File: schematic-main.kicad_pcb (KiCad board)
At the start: 2 copper layers, 97.6 x 72.5 mm, 77 parts, among them IC1 LM76202QPWPRQ1, J1 Conn_01x02, J2 Conn_01x03, J3 Conn_01x03_Pin, J6 Conn_01x04, P1 USB_C_Plug_USB2.0, U2 TPS62933, U3 USBLC6-2P6, U4 ESP32-S3FN8, U5 SN65HVD232, U6 PC817, U7 PC817, Y1 Crystal_GND24

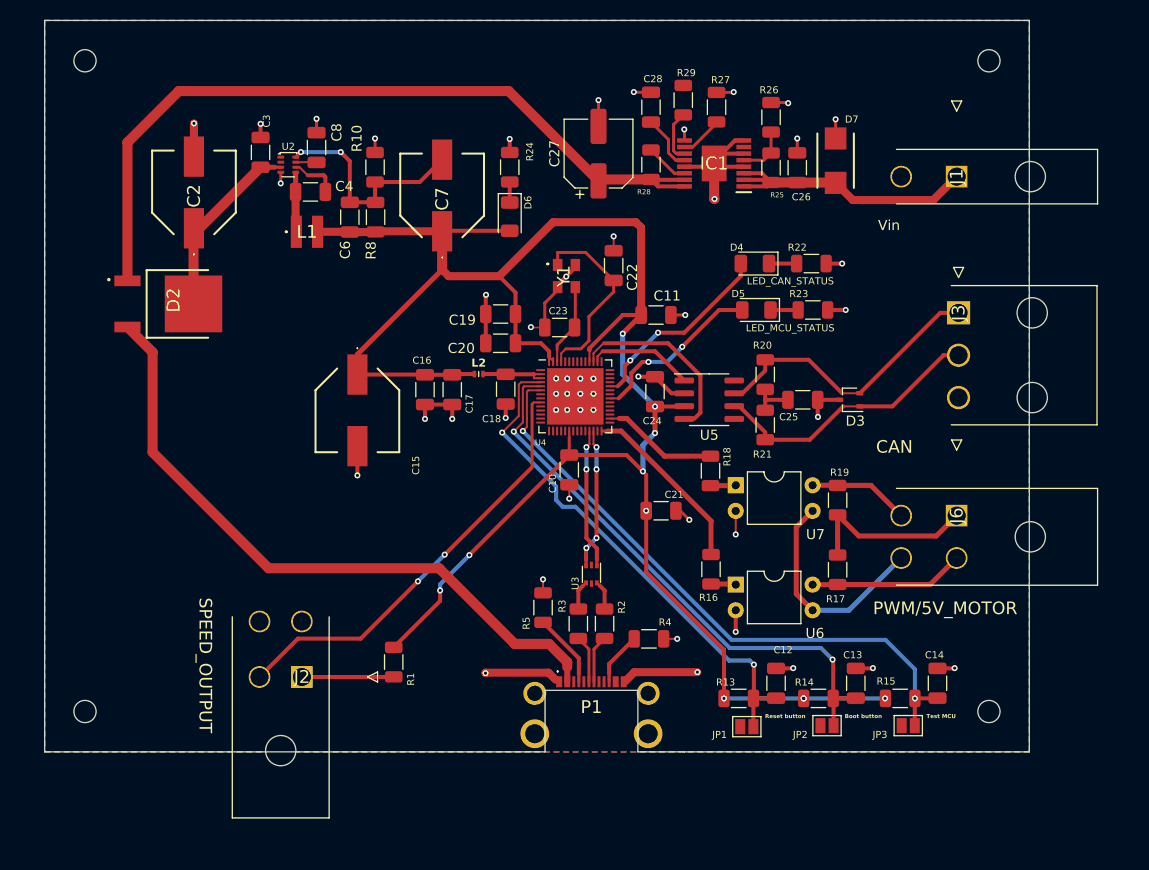
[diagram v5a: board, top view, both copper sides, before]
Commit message: Add test pins for: 3,3V, 5V, 12V and GND
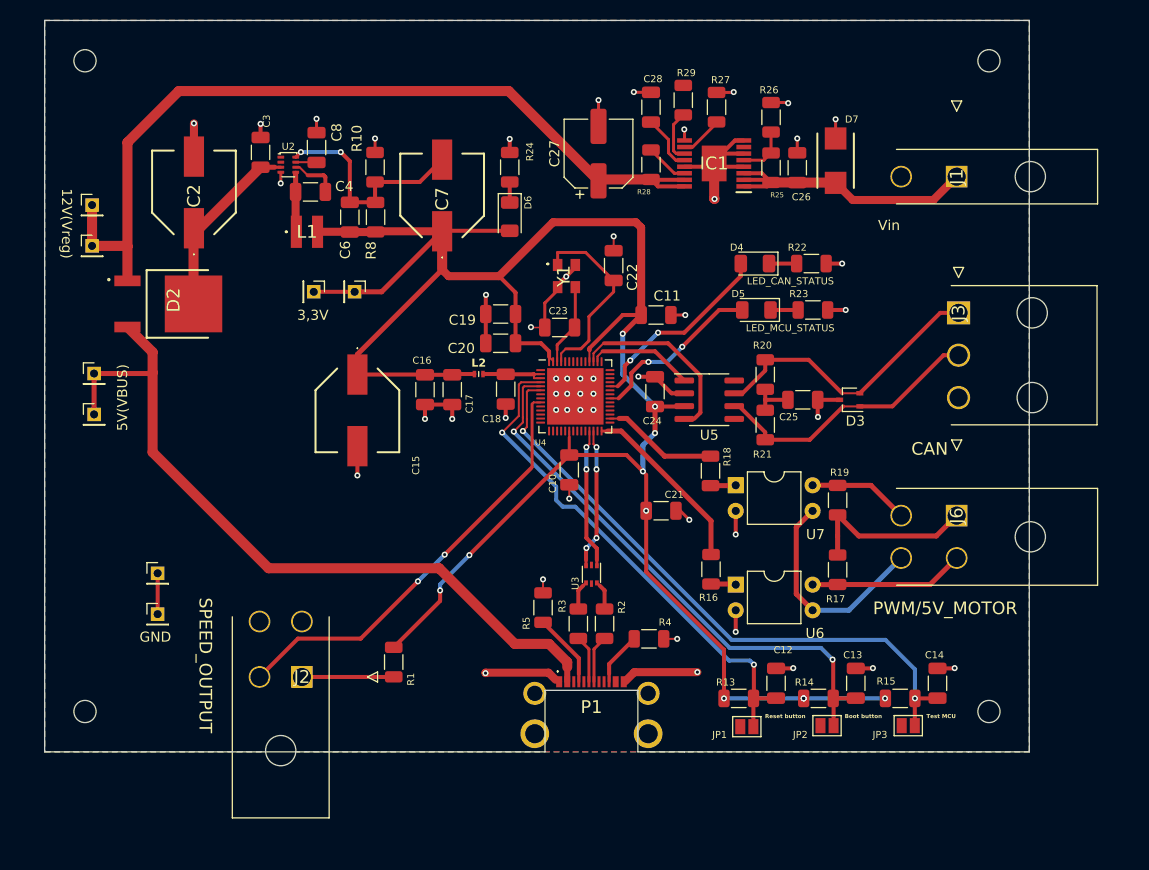
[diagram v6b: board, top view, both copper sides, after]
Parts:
- added TP1: +12V, Connector_PinHeader_2.00mm:PinHeader_1x01_P2.00mm_Vertical, F.Cu at (53.1, 70.0)
- added TP2: +12V, Connector_PinHeader_2.00mm:PinHeader_1x01_P2.00mm_Vertical, F.Cu at (53.1, 74.0)
- added TP3: +5V, Connector_PinHeader_2.00mm:PinHeader_1x01_P2.00mm_Vertical, F.Cu at (53.3, 86.7)
- added TP4: +5V, Connector_PinHeader_2.00mm:PinHeader_1x01_P2.00mm_Vertical, F.Cu at (53.3, 90.8)
- added TP5: +3,3V, Connector_PinHeader_2.00mm:PinHeader_1x01_P2.00mm_Vertical, F.Cu at (79.1, 78.6)
- added TP6: +3,3V, Connector_PinHeader_2.00mm:PinHeader_1x01_P2.00mm_Vertical, F.Cu at (75.1, 78.6)
- added TP7: GND, Connector_PinHeader_2.00mm:PinHeader_1x01_P2.00mm_Vertical, F.Cu at (59.6, 106.5)
- added TP8: GND, Connector_PinHeader_2.00mm:PinHeader_1x01_P2.00mm_Vertical, F.Cu at (59.6, 110.5)
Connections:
- net /Power /Vreg renamed /Vreg
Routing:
- net +3.3V: track 199.7 -> 215.0 mm
- net /VBUS: track 66.7 -> 76.6 mm
- net /Vreg: track 78.4 -> 86.0 mm
- net GND: track 108.9 -> 112.9 mm
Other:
- board text added: "12V(Vreg)"
- board text added: "3,3V"
- board text added: "5V(VBUS)"
- board text added: "GND"

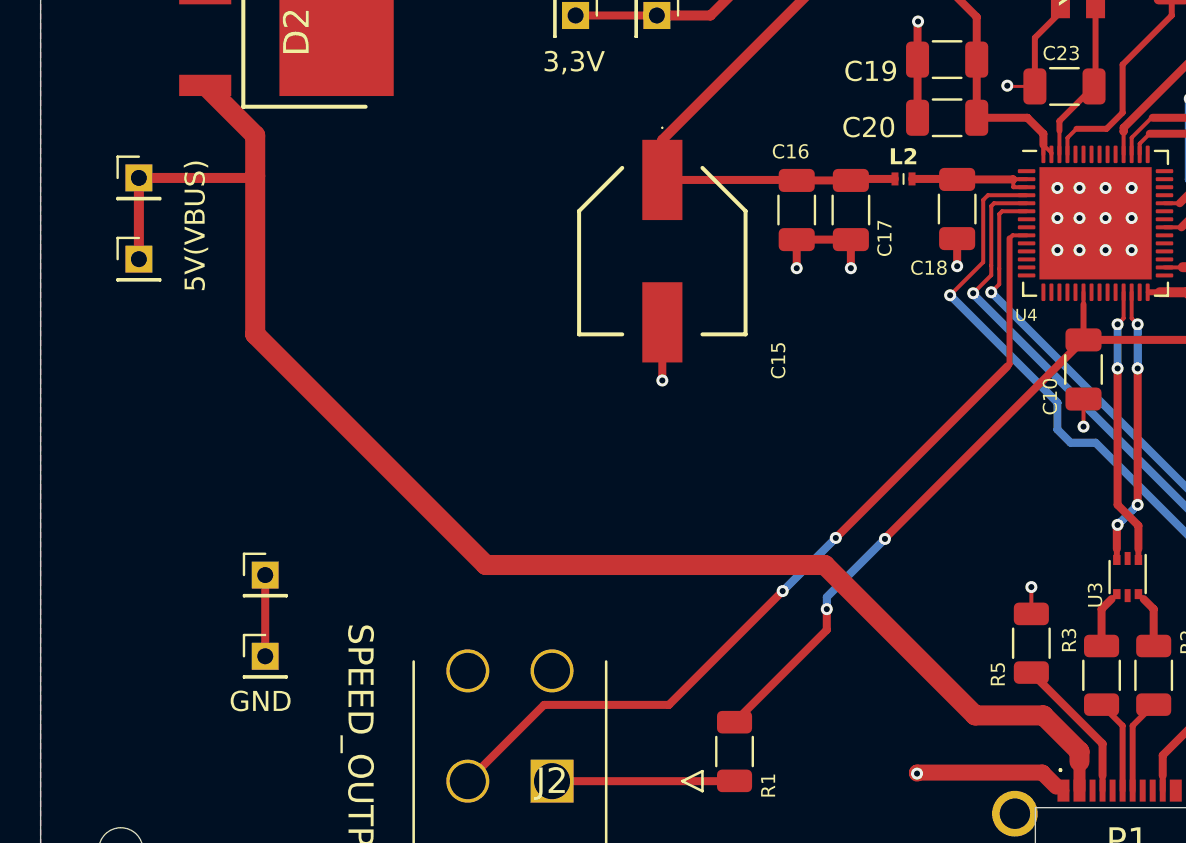
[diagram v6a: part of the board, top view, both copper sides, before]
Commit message: Add test pins for I/O MCU
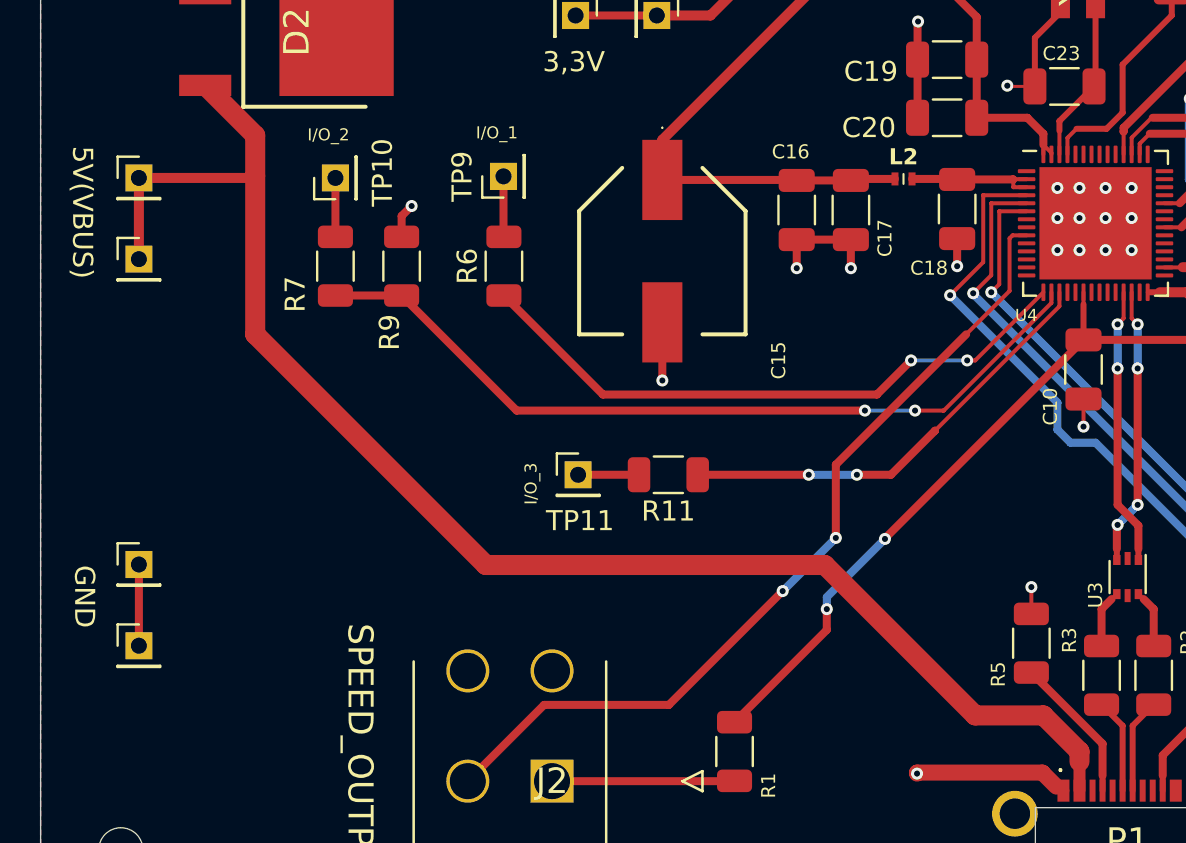
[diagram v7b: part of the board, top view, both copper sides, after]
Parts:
- added R11: R, Resistor_SMD:R_1206_3216Metric, F.Cu at (79.7, 101.5)
- added R6: R, Resistor_SMD:R_1206_3216Metric, F.Cu at (71.5, 91.1)
- added R7: R, Resistor_SMD:R_1206_3216Metric, F.Cu at (63.1, 91.1)
- added R9: R, Resistor_SMD:R_1206_3216Metric, F.Cu at (66.4, 91.1)
- added TP10: I/O_2, Connector_PinHeader_2.00mm:PinHeader_1x01_P2.00mm_Vertical, F.Cu at (63.1, 86.7)
- added TP11: I/O_3, Connector_PinHeader_2.00mm:PinHeader_1x01_P2.00mm_Vertical, F.Cu at (75.2, 101.5)
- added TP9: I/O_1, Connector_PinHeader_2.00mm:PinHeader_1x01_P2.00mm_Vertical, F.Cu at (71.5, 86.6)
- moved TP7 6.32 mm to (53.3, 106.0)
- moved TP8 6.32 mm to (53.3, 110.0)
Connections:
- U4 pad 15: unconnected-(U4-GPIO10/ADC1_CH9-Pad15) -> /IO/I/O_1_MCU
- U4 pad 16: unconnected-(U4-GPIO11/ADC2_CH0-Pad16) -> /IO/I/O_2_MCU
- U4 pad 17: unconnected-(U4-GPIO12/ADC2_CH1-Pad17) -> /IO/I/O_3_MCU
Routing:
- net /IO/I/O_2_MCU: track 0.00 -> 40.8 mm, vias 0 -> 2
- net /IO/I/O_1_MCU: track 0.00 -> 31.1 mm, vias 0 -> 2
- net /IO/I/O_3_MCU: track 0.00 -> 22.2 mm, vias 0 -> 2
- net Net-(R11-Pad2): track 0.00 -> 3.04 mm
- net Net-(R6-Pad2): track 0.00 -> 3.03 mm
- net Net-(R7-Pad1): track 0.00 -> 2.94 mm
- net GND: track 112.9 -> 114.7 mm, vias 50 -> 51
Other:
- board text added: "I/O_1"
- board text added: "I/O_2"
- board text added: "I/O_3"

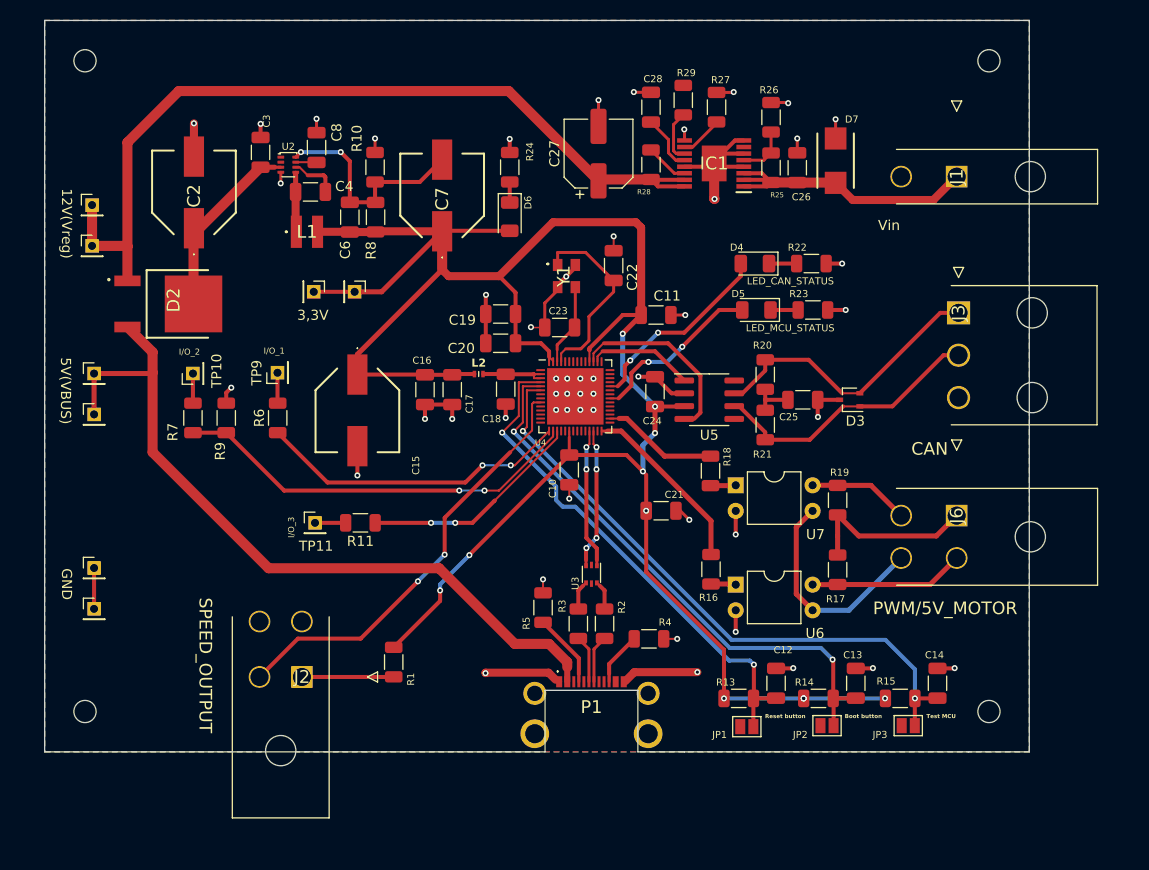
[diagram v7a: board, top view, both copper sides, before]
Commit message: Remake motor control driver
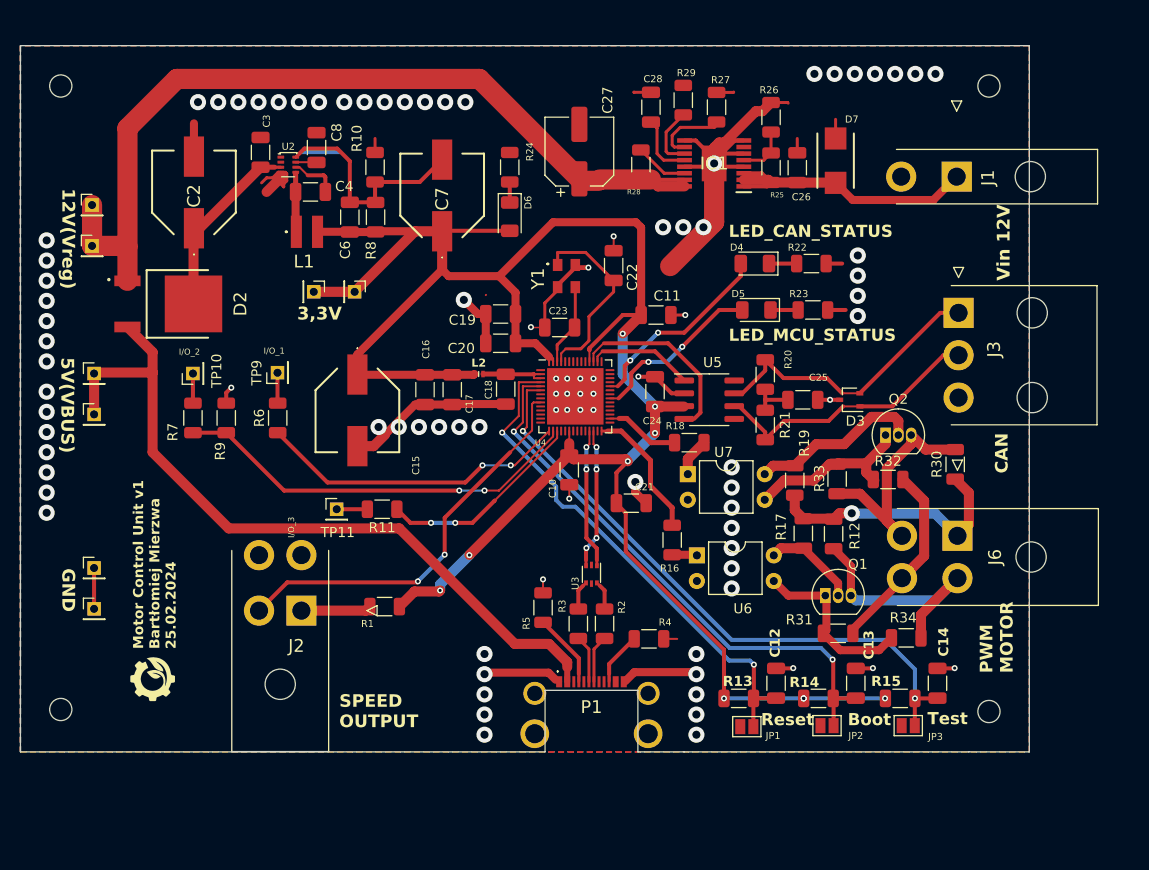
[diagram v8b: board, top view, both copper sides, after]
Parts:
- added Q1: 2N3904, Package_TO_SOT_THT:TO-92_Inline, F.Cu at (125.8, 108.7)
- added Q2: 2N3904, Package_TO_SOT_THT:TO-92_Inline, F.Cu at (131.8, 92.8)
- added R12: 1k0, Resistor_SMD:R_1206_3216Metric, F.Cu at (126.6, 102.6)
- added R30: 1k0, Resistor_SMD:R_1206_3216Metric, F.Cu at (138.7, 95.7)
- added R31: 0, Resistor_SMD:R_1206_3216Metric, F.Cu at (127.0, 112.5)
- added R32: 0, Resistor_SMD:R_1206_3216Metric, F.Cu at (132.0, 97.2)
- added R33: 1, Resistor_SMD:R_1206_3216Metric, F.Cu at (127.0, 97.2)
- added R34: 1, Resistor_SMD:R_1206_3216Metric, F.Cu at (133.8, 112.9)
- R17, R19: value 270 -> 1k
- moved J2 6.58 mm to (73.8, 110.2)
- moved R1 5.57 mm to (82.1, 109.8), turned to 0 degrees
- moved R17 4.95 mm to (123.6, 102.5)
- moved U7 4.88 mm to (112.2, 96.7)
- moved U6 4.82 mm to (113.0, 104.7)
- moved R16 4.82 mm to (110.6, 103.2)
- moved R19 4.68 mm to (122.8, 97.3)
- moved R18 3.50 mm to (112.3, 93.5), turned to 0 degrees
- moved H2 3.47 mm to (50.0, 58.2)
- moved C21 3.04 mm to (106.5, 99.5)
- moved R11 2.54 mm to (81.8, 100.2)
- moved TP11 2.54 mm to (77.3, 100.2)
- moved H1 2.50 mm to (142.0, 58.2)
- moved H3 2.41 mm to (50.0, 120.0)
- moved J6 2.00 mm to (138.9, 102.8)
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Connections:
- R17 pad 2: /PWM_MOTOR -> Net-(Q1-B)
- R19 pad 2: /MOTOR_ON_OFF -> Net-(Q2-B)
- U6 pad 3: /IO/GND_MOTOR -> Net-(Q1-E)
- U6 pad 4: /PWM_MOTOR -> Net-(Q1-B)
- U7 pad 3: /IO/GND_MOTOR -> Net-(Q2-E)
- U7 pad 4: /MOTOR_ON_OFF -> Net-(Q2-B)
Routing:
- net GND: track 114.7 -> 141.1 mm, vias 51 -> 92
- net Net-(Q1-E): track 0.00 -> 17.6 mm
- net Net-(Q2-E): track 0.00 -> 17.2 mm
- net Net-(Q2-B): track 0.00 -> 17.2 mm
- net /MOTOR_ON_OFF: track 10.0 -> 24.7 mm
- net Net-(Q1-B): track 0.00 -> 9.35 mm
- net /PWM_MOTOR: track 15.4 -> 24.4 mm
- net /IO/5V_MOTOR: track 17.5 -> 25.8 mm, vias 0 -> 1
- net /IO/PWM_MCU: track 17.8 -> 13.1 mm
- net Net-(U2-FB): track 22.2 -> 26.4 mm, vias 2 -> 0
- net /IO/MOTOR_ON_OFF_MCU: track 11.5 -> 7.50 mm
- net Net-(IC1-IMON): track 4.28 -> 7.39 mm
- net /IO/GND_MOTOR: track 22.1 -> 19.0 mm
- net +3.3V: track 215.0 -> 212.1 mm, vias 11 -> 10
- net /MCU/SPEED_OUTPUT: track 42.8 -> 40.1 mm
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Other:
- board size 97.6 x 72.5 mm -> 100 x 70 mm
- board text added: "Boot"
- board text added: "Motor Control Unit v1 Bartłomiej Mierzwa 25.02.2024"
- board text added: "PWM MOTOR"
- board text added: "Reset"
- board text added: "SPEED OUTPUT"
- board text added: "Test"
- board text added: "Vin 12V"
- board text removed: "Boot button"
- board text removed: "PWM/5V_MOTOR"
- board text removed: "Reset button"
- board text removed: "SPEED_OUTPUT"
- board text removed: "Test MCU"
- board text removed: "Vin"
